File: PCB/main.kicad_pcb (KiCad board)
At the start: 4 copper layers, 65.2 x 45.1 mm, 63 parts, among them J1 S20B-PADSS-1, J2 S20B-PADSS-1, J3 SWD, SW1 SPST, U1 XC6206P33, U3 MCP2558FD, U4 MCP2558FD, U5 STM32G0B1, U6 TPS54302, Y1 40M

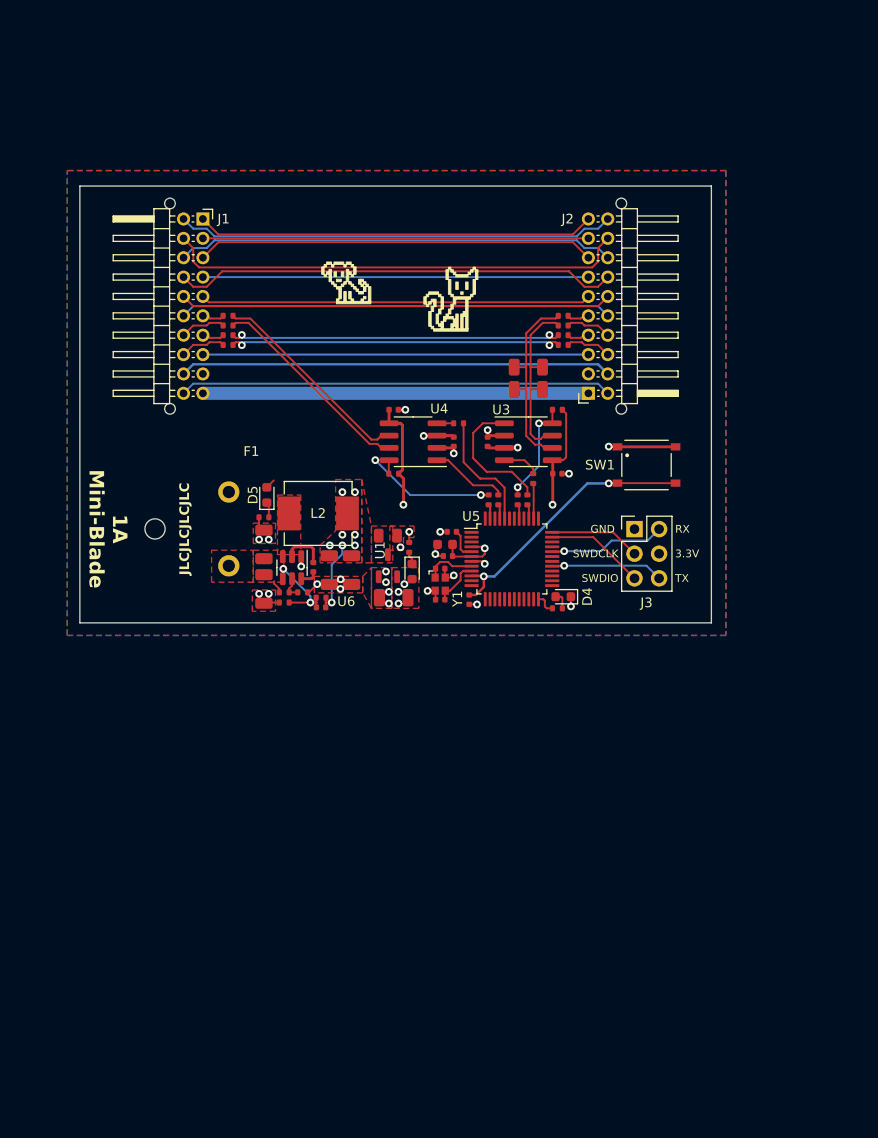
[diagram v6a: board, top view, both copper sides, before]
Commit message: Finish plane layout
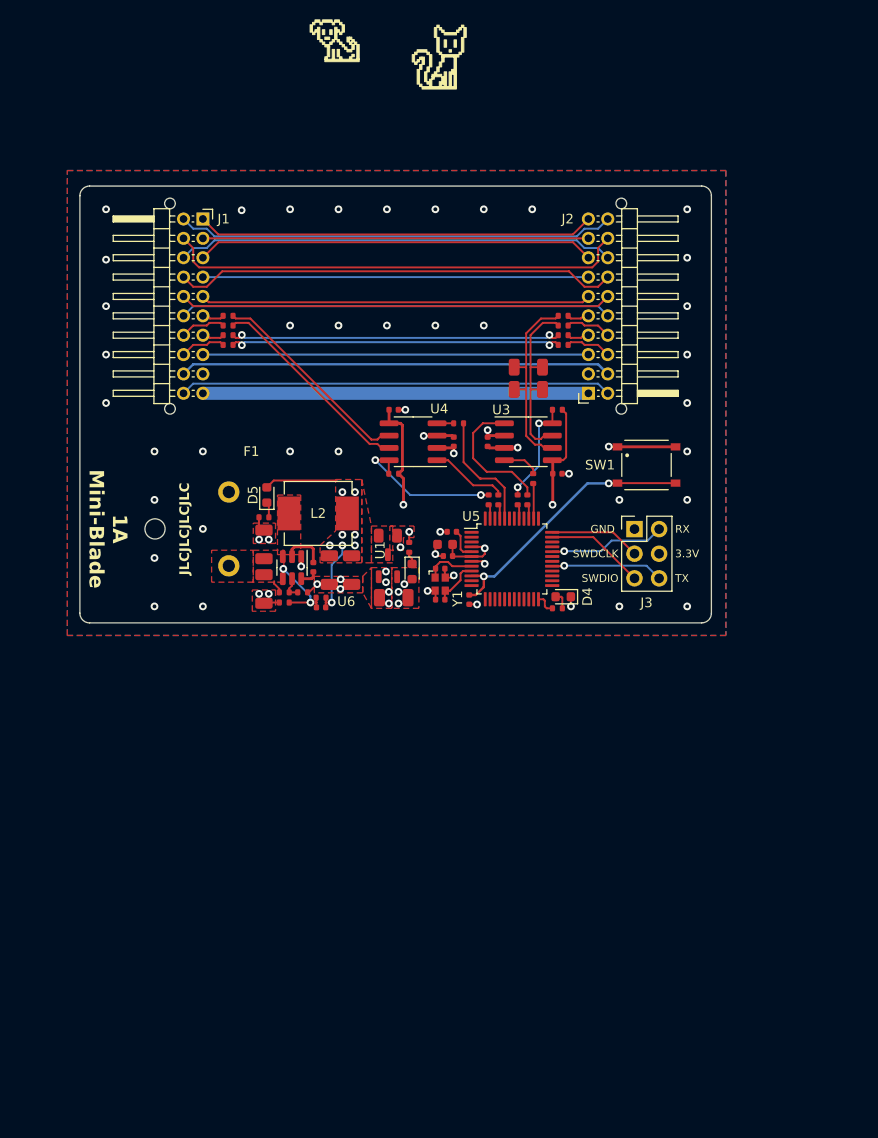
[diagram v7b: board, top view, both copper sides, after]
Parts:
- moved ART2 25.0 mm to (53.9, 12.2)
- moved ART1 25.0 mm to (64.4, 14.3)
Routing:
- net +5V: track 15.4 -> 21.8 mm
- net GND: vias 26 -> 62
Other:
- outline, holes or cut-outs redrawn

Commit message: Generate gerbers
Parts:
- added REF**: CMP-0066, libdb:CMP-0066, F.Cu at (50.6, 31.2)
- moved ART1 42.0 mm to (51.9, 54.4)
- moved ART2 37.0 mm to (61.2, 48.5)
- moved REF** 2.62 mm to (27.3, 73.1)
- moved REF** 2.61 mm to (94.3, 71.7)
- moved C12 0.96 mm to (58.7, 49.7), turned to 180 degrees
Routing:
- net GND: vias 62 -> 63
- added copper zone on In2.Cu, net GND
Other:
- board text added: "BMW F20 AHU CAN Relay v1.0 Richard Carter"
